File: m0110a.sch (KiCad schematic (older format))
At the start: 159 parts, among them U1 Teensy2.0_(C)

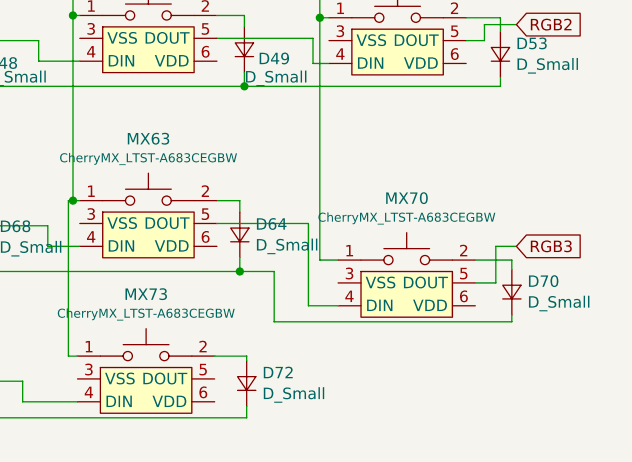
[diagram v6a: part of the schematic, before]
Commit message: connect the data rgb between rows
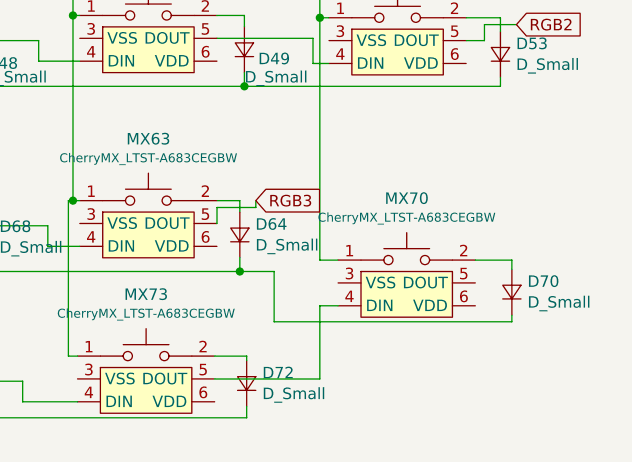
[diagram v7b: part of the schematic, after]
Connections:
- net RGB3: now also MX63.5 (DOUT); no longer MX70.5 (DOUT)
- net at MX70.4 (DIN): now also MX73.5 (DOUT); no longer MX63.5 (DOUT)
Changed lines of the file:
@@
 Wire Wire Line
 	22690 3620 22830 3620
-Wire Wire Line
-	23430 3520 23830 3520
-Wire Wire Line
-	23830 3520 23830 3880
-Wire Wire Line
-	23830 3880 23960 3880
-Wire Wire Line
-	24560 3780 24650 3780
-Wire Wire Line
-	24650 3780 24650 3620
-Wire Wire Line
-	24650 3620 24740 3620
-Text GLabel 24740 3620 2    50   Input ~ 0
+Text GLabel 23600 3420 2    50   Input ~ 0
 RGB3
 Text GLabel 4970 4320 0    50   Input ~ 0
@@
 	16600 3090 16600 2620
 Connection ~ 16600 2620
+Wire Wire Line
+	23600 3420 23600 3450
+Wire Wire Line
+	23600 3450 23430 3450
+Wire Wire Line
+	23430 3450 23430 3520
+Wire Wire Line
+	23420 4200 23880 4200
+Wire Wire Line
+	23880 4200 23880 3880
+Wire Wire Line
+	23880 3880 23960 3880
 $EndSCHEMATC

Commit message: start adding capacitors for the LEDs
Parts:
- added C? (x5): C_Small, symbol Device:C_Small
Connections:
- net GND: now also MX1.3 (VSS), MX10.3 (VSS), MX11.3 (VSS), MX12.3 (VSS), MX13.3 (VSS), MX14.3 (VSS), MX15.3 (VSS), MX16.3 (VSS), MX17.3 (VSS), MX18.3 (VSS), MX2.3 (VSS), MX3.3 (VSS), MX4.3 (VSS), MX5.3 (VSS), MX6.3 (VSS), MX7.3 (VSS), MX8.3 (VSS), MX9.3 (VSS), C?.1, C?.1, C?.1, C?.1, C?.1
- net VCC: now also MX13.6 (VDD), MX14.6 (VDD), MX18.6 (VDD), MX8.6 (VDD), MX9.6 (VDD), C?.2, C?.2, C?.2, C?.2, C?.2
- net RGBc: now reaches MX18.4 (DIN)
- net RGBc: now also U1.7 (PD0_INT0_SCL_OC0B)
